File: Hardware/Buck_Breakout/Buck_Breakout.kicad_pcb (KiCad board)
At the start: 2 copper layers, 25.4 x 12.7 mm, 10 parts, among them U1 AP62200WU

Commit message: Generate BOM for buck breakout
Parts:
- C2: value C -> 100nF
- R1: value R -> R1
- R2: value R -> R2
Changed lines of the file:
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@@
 		(tags "capacitor handsolder")
 		(property "Reference" "C1"
-			(at 0 -1.43 360)
+			(at 0 -1.43 0)
 			(layer "F.SilkS")
 			(effects
@@
 		)
 		(property "Value" "10uF"
-			(at 0 0 360)
+			(at 0 0 0)
 			(layer "F.Fab")
 			(effects
@@
 		)
 		(fp_text user "${REFERENCE}"
-			(at 0 0 360)
+			(at 0 0 0)
 			(layer "F.Fab")
 			(effects
@@
 			)
 		)
-		(property "Value" "R"
+		(property "Value" "R2"
 			(at 0 0 90)
 			(layer "F.Fab")
@@
 		(tags "capacitor handsolder")
 		(property "Reference" "C2"
-			(at -2.667 0 360)
-			(layer "F.SilkS")
-			(effects
-				(font
-					(size 1 1)
-					(thickness 0.15)
-				)
-			)
-		)
-		(property "Value" "C"
-			(at 0 0 360)
+			(at -2.667 0 0)
+			(layer "F.SilkS")
+			(effects
+				(font
+					(size 1 1)
+					(thickness 0.15)
+				)
+			)
+		)
+		(property "Value" "100nF"
+			(at 0 0 0)
 			(layer "F.Fab")
 			(effects
@@
 		)
 		(fp_text user "${REFERENCE}"
-			(at 0 0 360)
+			(at 0 0 0)
 			(layer "F.Fab")
 			(effects
@@
 		(tags "resistor handsolder")
 		(property "Reference" "R1"
-			(at -2.6435 0 360)
-			(layer "F.SilkS")
-			(effects
-				(font
-					(size 1 1)
-					(thickness 0.15)
-				)
-			)
-		)
-		(property "Value" "R"
-			(at 0 0 360)
+			(at -2.6435 0 0)
+			(layer "F.SilkS")
+			(effects
+				(font
+					(size 1 1)
+					(thickness 0.15)
+				)
+			)
+		)
+		(property "Value" "R1"
+			(at 0 0 0)
 			(layer "F.Fab")
 			(effects
@@
 		)
 		(fp_text user "${REFERENCE}"
-			(at 0 0 360)
+			(at 0 0 0)
 			(layer "F.Fab")
 			(effects
@@
 		(tags "capacitor handsolder")
 		(property "Reference" "C3"
-			(at 0 1.397 360)
+			(at 0 1.397 0)
 			(layer "F.SilkS")
 			(effects
@@
 		)
 		(property "Value" "22uF"
-			(at 0 0 360)
+			(at 0 0 0)
 			(layer "F.Fab")
 			(effects
@@
 		)
 		(fp_text user "${REFERENCE}"
-			(at 0 0 360)
-			(layer "F.Fab")
-			(effects
+			(at 0 0 0)
+			(layer "F.Fab")
+			(effects

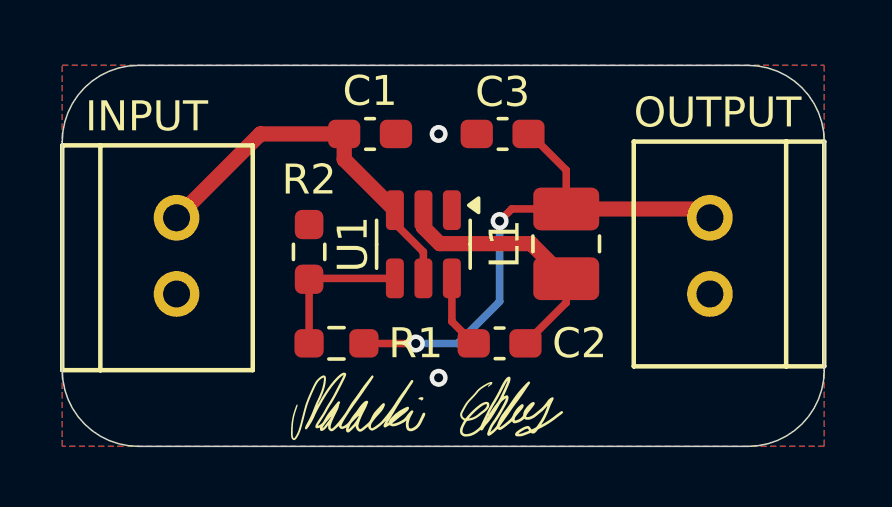
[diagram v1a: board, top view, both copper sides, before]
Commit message: Add second capacitor to buck breakout output
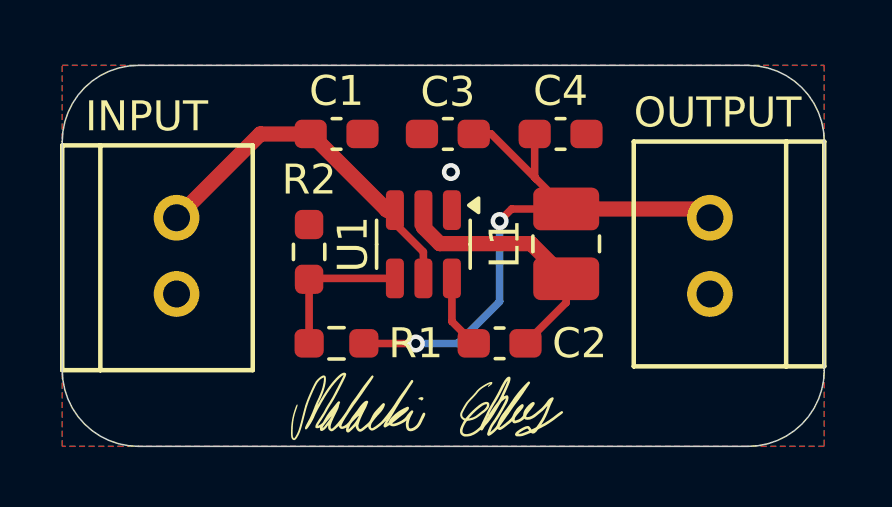
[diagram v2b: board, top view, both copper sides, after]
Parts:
- added C4: 22uF, Capacitor_SMD:C_0603_1608Metric_Pad1.08x0.95mm_HandSolder, F.Cu at (87.7, 53.1)
- moved C3 1.83 mm to (84.0, 53.1)
- moved C1 1.12 mm to (80.3, 53.1)
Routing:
- net OUTPUT: track 18.1 -> 20.7 mm
- net GND: vias 2 -> 1
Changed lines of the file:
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@@
 	(footprint "Capacitor_SMD:C_0603_1608Metric_Pad1.08x0.95mm_HandSolder"
 		(layer "F.Cu")
-		(at 81.3805 53.086)
+		(at 80.264 53.086)
 		(descr "Capacitor SMD 0603 (1608 Metric), square (rectangular) end terminal, IPC_7351 nominal with elongated pad for handsoldering. (Body size source: IPC-SM-782 page 76, https://www.pcb-3d.com/wordpress/wp-content/uploads/ipc-sm-782a_amendment_1_and_2.pdf), generated with kicad-footprint-generator")
 		(tags "capacitor handsolder")
@@
 	(footprint "Capacitor_SMD:C_0603_1608Metric_Pad1.08x0.95mm_HandSolder"
 		(layer "F.Cu")
+		(at 87.7305 53.086)
+		(descr "Capacitor SMD 0603 (1608 Metric), square (rectangular) end terminal, IPC_7351 nominal with elongated pad for handsoldering. (Body size source: IPC-SM-782 page 76, https://www.pcb-3d.com/wordpress/wp-content/uploads/ipc-sm-782a_amendment_1_and_2.pdf), generated with kicad-footprint-generator")
+		(tags "capacitor handsolder")
+		(property "Reference" "C4"
+			(at 0 -1.43 360)
+			(layer "F.SilkS")
+			(effects
+				(font
+					(size 1 1)
+					(thickness 0.15)
+				)
+			)
+		)
+		(property "Value" "22uF"
+			(at 0 1.43 360)
+			(layer "F.Fab")
+			(effects
+				(font
+					(size 1 1)
+					(thickness 0.15)
+				)
+			)
+		)
+		(property "Footprint" "Capacitor_SMD:C_0603_1608Metric_Pad1.08x0.95mm_HandSolder"
+			(at 0 0 0)
+			(unlocked yes)
+			(layer "F.Fab")
+			(hide yes)
+			(effects
+				(font
+					(size 1.27 1.27)
+					(thickness 0.15)
+				)
+			)
+		)
+		(property "Datasheet" ""
+			(at 0 0 0)
+			(unlocked yes)
+			(layer "F.Fab")
+			(hide yes)
+			(effects
+				(font
+					(size 1.27 1.27)
+					(thickness 0.15)
+				)
+			)
+		)
+		(property "Description" "Unpolarized capacitor"
+			(at 0 0 0)
+			(unlocked yes)
+			(layer "F.Fab")
+			(hide yes)
+			(effects
+				(font
+					(size 1.27 1.27)
+					(thickness 0.15)
+				)
+			)
+		)
+		(property ki_fp_filters "C_*")
+		(sheetname "Root")
+		(sheetfile "Buck_Breakout.kicad_sch")
+		(attr smd)
+		(fp_line
+			(start -0.146267 -0.51)
+			(end 0.146267 -0.51)
+			(stroke
+				(width 0.12)
+				(type solid)
+			)
+			(layer "F.SilkS")
+		)
+		(fp_line
+			(start -0.146267 0.51)
+			(end 0.146267 0.51)
+			(stroke
+				(width 0.12)
+				(type solid)
+			)
+			(layer "F.SilkS")
+		)
+		(fp_line
+			(start -1.65 -0.73)
+			(end 1.65 -0.73)
+			(stroke
+				(width 0.05)
+				(type solid)
+			)
+			(layer "F.CrtYd")
+		)
+		(fp_line
+			(start -1.65 0.73)
+			(end -1.65 -0.73)
+			(stroke
+				(width 0.05)
+				(type solid)
+			)
+			(layer "F.CrtYd")
+		)
+		(fp_line
+			(start 1.65 -0.73)
+			(end 1.65 0.73)
+			(stroke
+				(width 0.05)
+				(type solid)
+			)
+			(layer "F.CrtYd")
+		)
+		(fp_line
+			(start 1.65 0.73)
+			(end -1.65 0.73)
+			(stroke
+				(width 0.05)
+				(type solid)
+			)
+			(layer "F.CrtYd")
+		)
+		(fp_line
+			(start -0.8 -0.4)
+			(end 0.8 -0.4)
+			(stroke
+				(width 0.1)
+				(type solid)
+			)
+			(layer "F.Fab")
+		)
+		(fp_line
+			(start -0.8 0.4)
+			(end -0.8 -0.4)
+			(stroke
+				(width 0.1)
+				(type solid)
+			)
+			(layer "F.Fab")
+		)
+		(fp_line
+			(start 0.8 -0.4)
+			(end 0.8 0.4)
+			(stroke
+				(width 0.1)
+				(type solid)
+			)
+			(layer "F.Fab")
+		)
+		(fp_line
+			(start 0.8 0.4)
+			(end -0.8 0.4)
+			(stroke
+				(width 0.1)
+				(type solid)
+			)
+			(layer "F.Fab")
+		)
+		(fp_text user "${REFERENCE}"
+			(at 0 0 360)
+			(layer "F.Fab")
+			(effects
+				(font
+					(size 0.4 0.4)
+					(thickness 0.06)
+				)
+			)
+		)
+		(pad "1" smd roundrect
+			(at -0.8625 0)
+			(size 1.075 0.95)
+			(layers "F.Cu" "F.Paste" "F.Mask")
+			(roundrect_rratio 0.25)
+			(net 5 "OUTPUT")
+			(pintype "passive")
+		)
+		(pad "2" smd roundrect
+			(at 0.8625 0)
+			(size 1.075 0.95)
+			(layers "F.Cu" "F.Paste" "F.Mask")
+			(roundrect_rratio 0.25)
+			(net 2 "GND")
+			(pintype "passive")
+		)
+		(model "${KICAD8_3DMODEL_DIR}/Capacitor_SMD.3dshapes/C_0603_1608Metric.wrl"
+			(offset
+				(xyz 0 0 0)
+			)
+			(scale
+				(xyz 1 1 1)
+			)
+			(rotate
+				(xyz 0 0 0)
+			)
+		)
+	)
+	(footprint "Capacitor_SMD:C_0603_1608Metric_Pad1.08x0.95mm_HandSolder"
+		(layer "F.Cu")
 		(at 85.6985 60.0655 180)
 		(descr "Capacitor SMD 0603 (1608 Metric), square (rectangular) end terminal, IPC_7351 nominal with elongated pad for handsoldering. (Body size source: IPC-SM-782 page 76, https://www.pcb-3d.com/wordpress/wp-content/uploads/ipc-sm-782a_amendment_1_and_2.pdf), generated with kicad-footprint-generator")
@@
 	(footprint "Capacitor_SMD:C_0603_1608Metric_Pad1.08x0.95mm_HandSolder"
 		(layer "F.Cu")
-		(at 85.799 53.086 180)
+		(at 83.9735 53.086 180)
 		(descr "Capacitor SMD 0603 (1608 Metric), square (rectangular) end terminal, IPC_7351 nominal with elongated pad for handsoldering. (Body size source: IPC-SM-782 page 76, https://www.pcb-3d.com/wordpress/wp-content/uploads/ipc-sm-782a_amendment_1_and_2.pdf), generated with kicad-footprint-generator")
 		(tags "capacitor handsolder")
@@
 	)
 	(segment
+		(start 77.724 53.086)
+		(end 79.4015 53.086)
+		(width 0.508)
+		(layer "F.Cu")
+		(net 1)
+	)
+	(segment
 		(start 82.2085 56.0685)
 		(end 82.2085 55.626)
@@
 	)
 	(segment
-		(start 80.518 53.086)
-		(end 80.518 53.9355)
+		(start 79.4015 53.086)
+		(end 81.9415 55.626)
 		(width 0.508)
 		(layer "F.Cu")
@@
 	)
 	(segment
-		(start 80.518 53.9355)
+		(start 81.9415 55.626)
 		(end 82.2085 55.626)
-		(width 0.508)
-		(layer "F.Cu")
-		(net 1)
-	)
-	(segment
-		(start 77.724 53.086)
-		(end 80.518 53.086)
 		(width 0.508)
 		(layer "F.Cu")
@@
 	)
 	(via
-		(at 83.6665 61.214)
+		(at 84.074 54.356)
 		(size 0.6)
 		(drill 0.3)
@@
 		(net 2)
 	)
-	(via
-		(at 83.6665 53.086)
-		(size 0.6)
-		(drill 0.3)
-		(layers "F.Cu" "B.Cu")
-		(free yes)
-		(net 2)
-	)
 	(segment
 		(start 84.836 60.0655)
@@
 	)
 	(segment
+		(start 86.90475 54.57325)
+		(end 87.9185 55.587)
+		(width 0.254)
+		(layer "F.Cu")
+		(net 5)
+	)
+	(segment
 		(start 86.1 55.587)
 		(end 85.6985 55.9885)
@@
 	)
 	(segment
-		(start 87.9185 54.29)
-		(end 86.7145 53.086)
+		(start 84.836 53.086)
+		(end 85.4175 53.086)
+		(width 0.254)
+		(layer "F.Cu")
+		(net 5)
+	)
+	(segment
+		(start 85.4175 53.086)
+		(end 86.90475 54.57325)
 		(width 0.254)
 		(layer "F.Cu")
@@
 	)
 	(segment
-		(start 87.9185 55.587)
-		(end 87.9185 54.29)
+		(start 86.868 53.086)
+		(end 86.868 54.5365)
 		(width 0.254)
 		(layer "F.Cu")
@@
 	)
 	(segment
-		(start 86.7145 53.086)
-		(end 86.6615 53.086)
+		(start 86.868 54.5365)
+		(end 86.90475 54.57325)
 		(width 0.254)
 		(layer "F.Cu")
